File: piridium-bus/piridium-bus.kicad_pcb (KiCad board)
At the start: 4 copper layers, 90.2 x 95.9 mm, 163 parts, among them J1 EPS, J2 INHIBITS, J3 MODEM UART, J4 ANT, J5 PAYLOAD, J6 IN1, J7 IN2, J8 IN1, J9 IN2, Q1 DMP3015LSSQ, Q10 DMP3015LSSQ, Q11 2N7002, Q12 2N7002, Q13 DMP3015LSSQ, Q14 2N7002, Q2 Si4186DY, Q3 DMP3015LSSQ, Q4 Si4186DY, Q5 DMP3015LSSQ, Q6 DMP3015LSSQ, Q7 2N7002, Q8 DMP3015LSSQ, Q9 2N7002, U1 LM1117-3.3, U10 LT3652EMSE, U11 INA180A3, U12 LT3652EMSE, U13 INA180A3, U14 SN74LVC1G14DBV, U15 MAX4373F, U16 SN74LVC1G14DBV, U17 MAX4373F, U2 MAX6369, U3 TPS54394RSAR, U4 INA180A3, U5 74HC126, U6 DS3232M, U7 MAX6035xxUR30, U8 MCP3208, U9 INA180A3

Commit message: pull down on/off instead of up
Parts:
- removed the R27 at (150.9, 114.3)
- R26: value 22K -> 10K; footprint Resistor_SMD:R_1206_3216Metric -> Resistor_SMD:R_0805_2012Metric; moved to B.Cu
- moved R26 14.9 mm to (138.2, 109.0), turned to 90 degrees
- renumbered R28 to R27, R29 to R28, R30 to R29, R31 to R30, R32 to R31, R33 to R32, R34 to R33, R35 to R34, R36 to R35, R37 to R36, R38 to R37, R39 to R38, R40 to R39, R41 to R40, R42 to R41, R43 to R42, R44 to R43, R45 to R44, R46 to R45, R47 to R46, R48 to R47, R49 to R48, R50 to R49, R51 to R50, R52 to R51
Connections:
- R26 pad 1: +5VP -> S_MODEM_ON_OFF
- R26 pad 2: S_MODEM_ON_OFF -> GND
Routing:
- net S_MODEM_ON_OFF: track 59.4 -> 45.1 mm, vias 2 -> 1
- net GND: track 104.4 -> 101.0 mm, vias 57 -> 58

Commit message: final trace edits
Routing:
- net Net-(C30-Pad1): track 64.6 -> 66.5 mm
- net Net-(C23-Pad1): track 227.1 -> 226.0 mm
- net +BATT: track 81.3 -> 80.5 mm

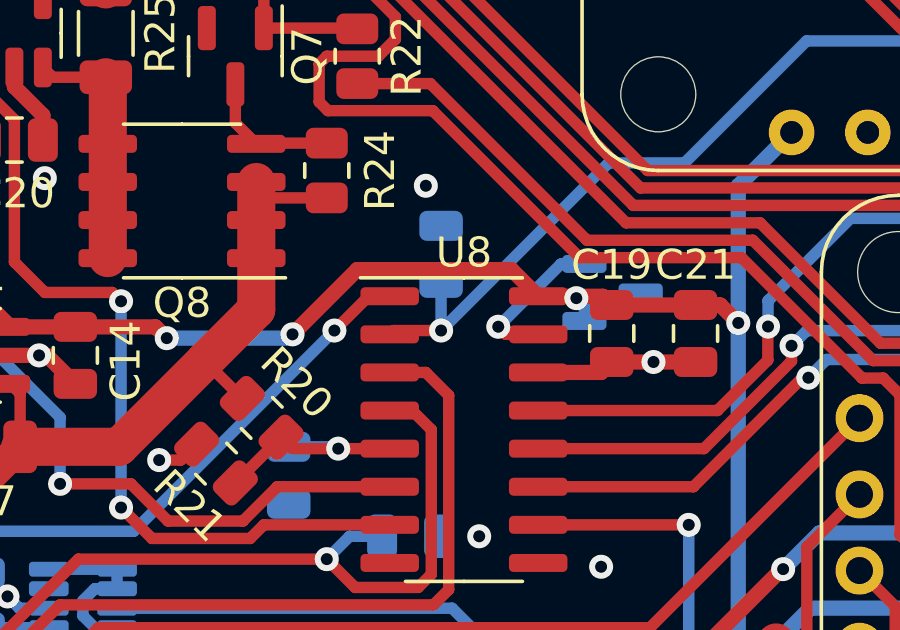
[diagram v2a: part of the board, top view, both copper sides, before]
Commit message: fix max6035 dropout
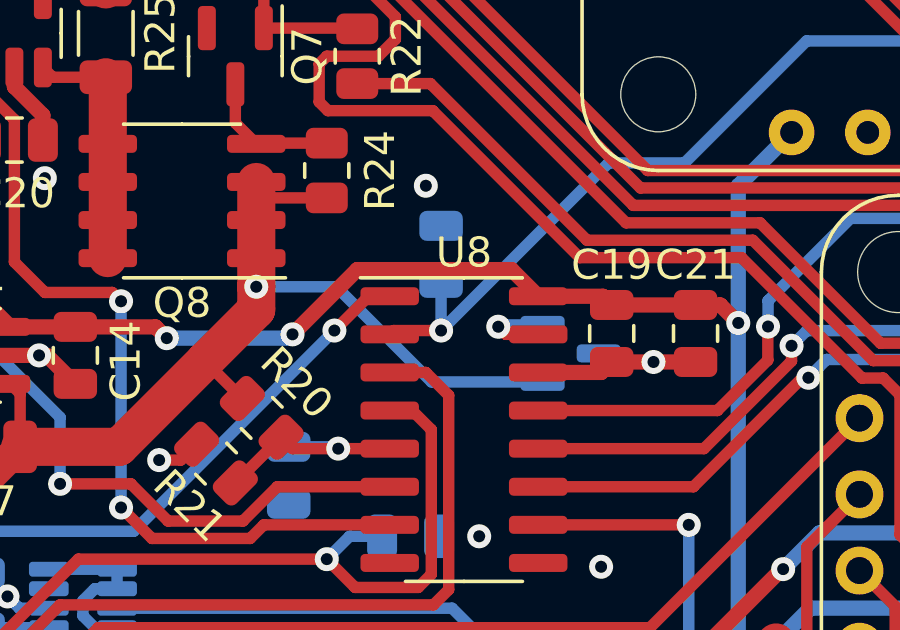
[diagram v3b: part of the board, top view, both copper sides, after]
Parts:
- moved U7 2.47 mm to (152.7, 78.7)
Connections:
- U7 pad 1: +3.3V -> +BATT
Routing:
- net +BATT: track 80.5 -> 91.4 mm, vias 1 -> 2
- net Net-(U7-Pad2): track 5.18 -> 2.94 mm
- net +3.3V: track 170.1 -> 169.2 mm, vias 9 -> 8
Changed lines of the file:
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@@
   )
   (footprint "Package_TO_SOT_SMD:SOT-23" (layer "B.Cu")
-    (at 154.051 76.708)
+    (at 152.654 78.74)
     (descr "SOT, 3 Pin (https://www.jedec.org/system/files/docs/to-236h.pdf variant AB), generated with kicad-footprint-generator ipc_gullwing_generator.py")
     (tags "SOT TO_SOT_SMD")
@@
     (fp_line (start 0.65 -1.45) (end -0.65 -1.45) (layer "B.Fab") (width 0.1))
     (pad "1" smd roundrect (at -0.9375 0.95) (size 1.475 0.6) (layers "B.Cu" "B.Paste" "B.Mask") (roundrect_rratio 0.25)
-      (net 1 "+3.3V") (pinfunction "IN") (pintype "power_in"))
+      (net 51 "+BATT") (pinfunction "IN") (pintype "power_in"))
     (pad "2" smd roundrect (at -0.9375 -0.95) (size 1.475 0.6) (layers "B.Cu" "B.Paste" "B.Mask") (roundrect_rratio 0.25)
       (net 135 "Net-(U7-Pad2)") (pinfunction "OUT") (pintype "power_out"))
@@
   (via (at 158.242 96.012) (size 0.8) (drill 0.4) (layers "F.Cu" "B.Cu") (net 1))
   (via (at 123.698 97.282) (size 0.8) (drill 0.4) (layers "F.Cu" "B.Cu") (net 1))
-  (via (at 152.8445 76.8985) (size 0.8) (drill 0.4) (layers "F.Cu" "B.Cu") (net 1))
   (via (at 126.111 86.233) (size 0.8) (drill 0.4) (layers "F.Cu" "B.Cu") (net 1))
   (segment (start 124.46 96.52) (end 123.698 97.282) (width 0.508) (layer "B.Cu") (net 1))
@@
   (segment (start 158.242 73.152) (end 160.02 71.374) (width 0.508) (layer "B.Cu") (net 1))
   (segment (start 163.569 110.093) (end 164.823 108.839) (width 0.508) (layer "B.Cu") (net 1))
-  (segment (start 152.8445 76.8985) (end 153.1135 77.1675) (width 0.381) (layer "B.Cu") (net 1))
   (segment (start 129.286 79.6235) (end 129.286 81.788) (width 0.508) (layer "B.Cu") (net 1))
   (segment (start 126.111 76.581) (end 128.905 76.581) (width 0.508) (layer "B.Cu") (net 1))
@@
   (segment (start 163.569 127.905) (end 163.569 110.093) (width 0.508) (layer "B.Cu") (net 1))
   (segment (start 139.192 78.232) (end 143.256 78.232) (width 0.508) (layer "B.Cu") (net 1))
-  (segment (start 153.1135 77.1675) (end 153.1135 77.658) (width 0.381) (layer "B.Cu") (net 1))
   (segment (start 181.2905 98.933) (end 182.118 99.7605) (width 0.381) (layer "F.Cu") (net 2))
   (segment (start 162.283 129.159) (end 162.283 126.619) (width 1.27) (layer "F.Cu") (net 2))
@@
   (segment (start 137.602 81.854) (end 140.462 78.994) (width 1.27) (layer "F.Cu") (net 51))
   (segment (start 132.08 84.0785) (end 134.3045 81.854) (width 1.016) (layer "F.Cu") (net 51))
-  (segment (start 142.175 77.281) (end 142.175 75.565) (width 1.27) (layer "F.Cu") (net 51))
+  (segment (start 142.175 77.281) (end 142.175 76.519) (width 1.27) (layer "F.Cu") (net 51))
   (segment (start 132.08 86.868) (end 132.08 84.0785) (width 1.016) (layer "F.Cu") (net 51))
   (segment (start 134.3045 80.081) (end 133.9795 79.756) (width 0.381) (layer "F.Cu") (net 51))
   (segment (start 130.81 88.138) (end 132.08 86.868) (width 1.016) (layer "F.Cu") (net 51))
+  (segment (start 142.175 76.519) (end 142.175 75.565) (width 1.27) (layer "F.Cu") (net 51))
   (segment (start 144.526 73.5565) (end 142.7065 73.5565) (width 0.381) (layer "F.Cu") (net 51))
   (segment (start 140.462 78.994) (end 142.175 77.281) (width 1.27) (layer "F.Cu") (net 51))
@@
   (segment (start 134.3045 81.854) (end 134.3045 80.081) (width 0.381) (layer "F.Cu") (net 51))
   (via (at 130.81 88.138) (size 1) (drill 0.5) (layers "F.Cu" "B.Cu") (net 51))
+  (via (at 142.175 76.519) (size 0.8) (drill 0.4) (layers "F.Cu" "B.Cu") (net 51))
   (segment (start 125.038 119.3045) (end 125.038 99.244) (width 1.016) (layer "B.Cu") (net 51))
   (segment (start 130.708 90.156) (end 129.62 90.156) (width 0.508) (layer "B.Cu") (net 51))
@@
   (segment (start 126.492 97.79) (end 126.492 91.44) (width 1.016) (layer "B.Cu") (net 51))
   (segment (start 125.1135 119.38) (end 125.1135 123.444) (width 1.016) (layer "B.Cu") (net 51))
+  (segment (start 148.016 79.69) (end 151.7165 79.69) (width 0.381) (layer "B.Cu") (net 51))
   (segment (start 125.1135 119.38) (end 125.038 119.3045) (width 1.016) (layer "B.Cu") (net 51))
   (segment (start 125.038 99.244) (end 126.492 97.79) (width 1.016) (layer "B.Cu") (net 51))
   (segment (start 129.62 90.156) (end 128.27 91.506) (width 0.508) (layer "B.Cu") (net 51))
   (segment (start 127.7195 114.3) (end 125.222 114.3) (width 0.762) (layer "B.Cu") (net 51))
+  (segment (start 142.175 76.519) (end 144.845 76.519) (width 0.381) (layer "B.Cu") (net 51))
+  (segment (start 144.845 76.519) (end 148.016 79.69) (width 0.381) (layer "B.Cu") (net 51))
   (segment (start 126.492 91.44) (end 129.794 88.138) (width 1.016) (layer "B.Cu") (net 51))
   (segment (start 129.794 88.138) (end 130.81 88.138) (width 1.016) (layer "B.Cu") (net 51))
@@
   (segment (start 150.495 78.105) (end 151.573 78.105) (width 0.381) (layer "F.Cu") (net 135))
   (via (at 150.241 77.851) (size 0.8) (drill 0.4) (layers "F.Cu" "B.Cu") (net 135))
-  (segment (start 152.334 75.758) (end 153.1135 75.758) (width 0.381) (layer "B.Cu") (net 135))
-  (segment (start 150.241 77.851) (end 152.334 75.758) (width 0.381) (layer "B.Cu") (net 135))
+  (segment (start 150.241 77.851) (end 150.302 77.79) (width 0.381) (layer "B.Cu") (net 135))
+  (segment (start 150.302 77.79) (end 151.7165 77.79) (width 0.381) (layer "B.Cu") (net 135))
   (segment (start 185.42 107.2255) (end 187.2845 107.2255) (width 0.381) (layer "F.Cu") (net 136))
   (segment (start 186.944 90.3685) (end 185.354 88.7785) (width 0.381) (layer "F.Cu") (net 136))
